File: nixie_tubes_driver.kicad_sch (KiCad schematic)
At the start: 3 parts, among them U5 CD40109BPW, U6 HV5122PG-G, U7 HV5122PG-G

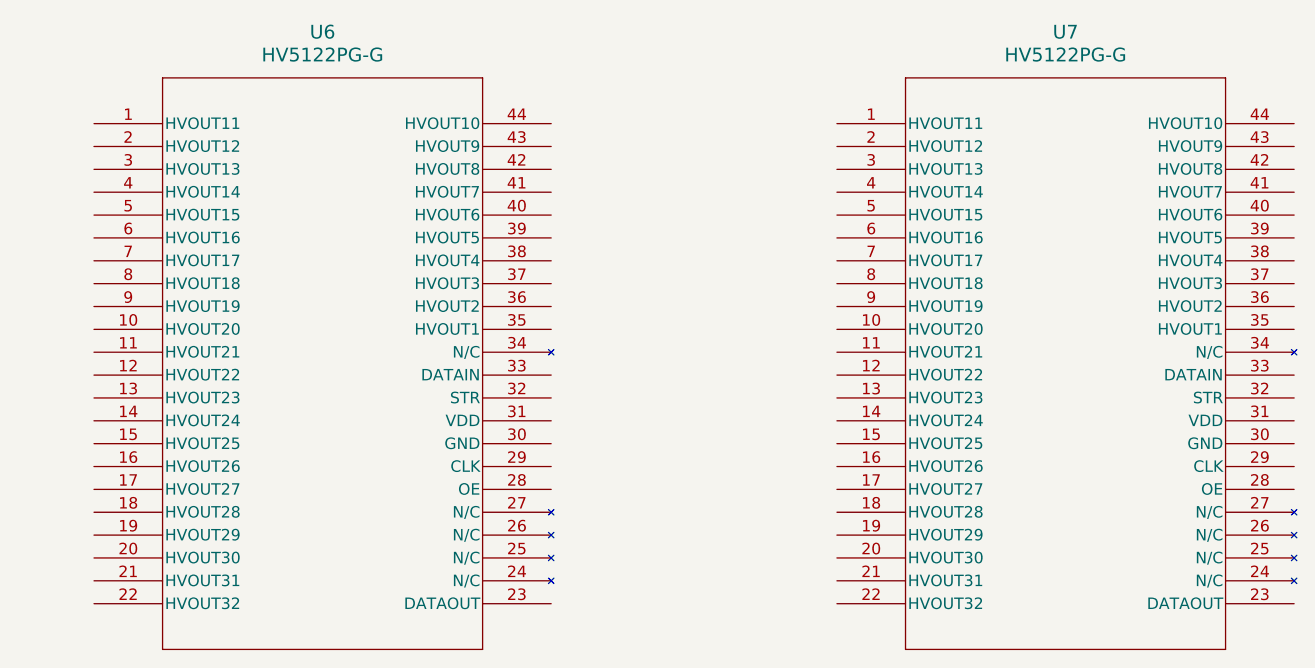
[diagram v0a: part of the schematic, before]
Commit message: Create symbol & footprint libraries
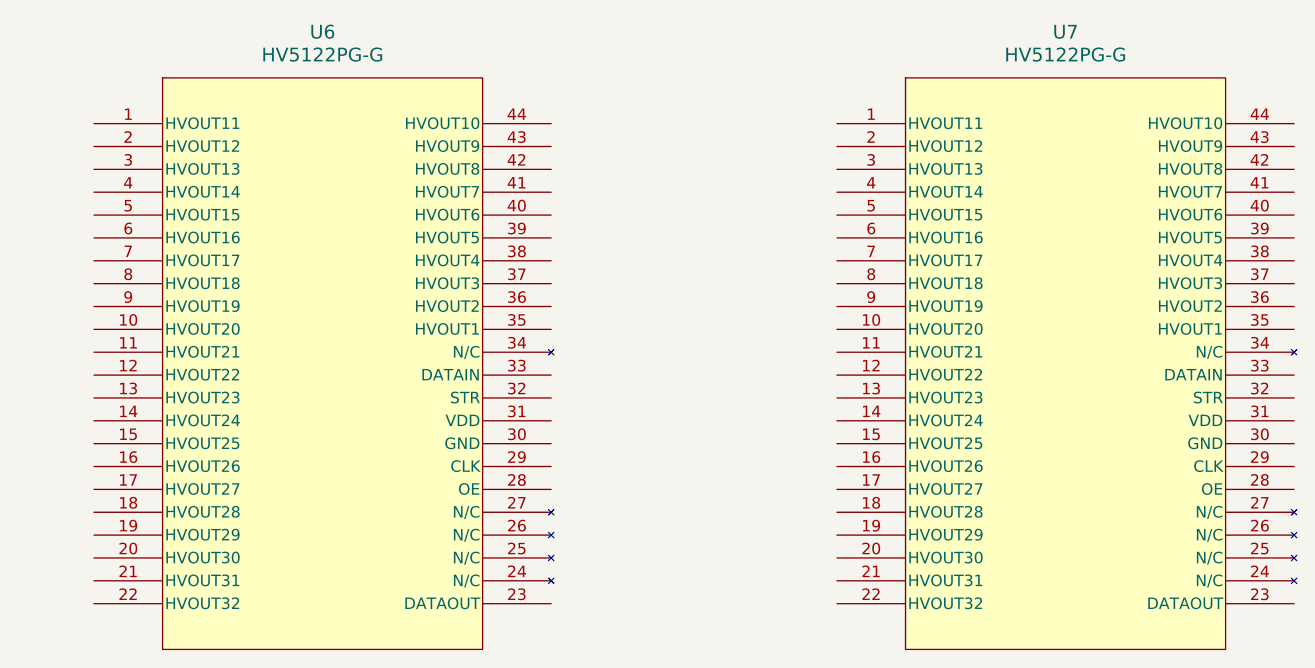
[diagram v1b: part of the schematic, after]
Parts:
- U6, U7: footprint HV5122PG-G:QFP44_10x10MC_MCH -> eclectronics_nixie_footprints:QFP44_10x10MC_MCH; symbol HV5122PG-G:HV5122PG-G -> electronics_nixie_lib:HV5122PG-G 32-Channel Shift Register; DigkeyPN (none) -> HV5122PG-G-ND; LCSCPN (none) -> C637042; MFN (none) -> Microchip Technology; MPN (none) -> HV5122PG-G
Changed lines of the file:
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@@
 	(paper "A4")
 	(symbol
-		(lib_id "HV5122PG-G:HV5122PG-G")
+		(lib_id "electronics_nixie_lib:HV5122PG-G 32-Channel Shift Register ")
 		(at 93.98 77.47 0)
 		(unit 1)
@@
 			)
 		)
-		(property "Footprint" "HV5122PG-G:QFP44_10x10MC_MCH"
+		(property "Footprint" "eclectronics_nixie_footprints:QFP44_10x10MC_MCH"
 			(at 93.98 77.47 0)
 			(effects
@@
 			)
 		)
-		(property "Datasheet" "HV5122PG-G"
+		(property "Datasheet" "https://ww1.microchip.com/downloads/en/DeviceDoc/20005418B.pdf"
 			(at 93.98 77.47 0)
 			(effects
@@
 		)
 		(property "Description" ""
+			(at 93.98 77.47 0)
+			(effects
+				(font
+					(size 1.27 1.27)
+				)
+				(hide yes)
+			)
+		)
+		(property "MFN" "Microchip Technology"
+			(at 93.98 77.47 0)
+			(effects
+				(font
+					(size 1.27 1.27)
+				)
+				(hide yes)
+			)
+		)
+		(property "MPN" "HV5122PG-G"
+			(at 93.98 77.47 0)
+			(effects
+				(font
+					(size 1.27 1.27)
+				)
+				(hide yes)
+			)
+		)
+		(property "DigkeyPN" "HV5122PG-G-ND"
+			(at 93.98 77.47 0)
+			(effects
+				(font
+					(size 1.27 1.27)
+				)
+				(hide yes)
+			)
+		)
+		(property "LCSCPN" "C637042"
 			(at 93.98 77.47 0)
 			(effects
@@
 	)
 	(symbol
-		(lib_id "HV5122PG-G:HV5122PG-G")
+		(lib_id "electronics_nixie_lib:HV5122PG-G 32-Channel Shift Register ")
 		(at 176.53 77.47 0)
 		(unit 1)
@@
 			)
 		)
-		(property "Footprint" "HV5122PG-G:QFP44_10x10MC_MCH"
+		(property "Footprint" "eclectronics_nixie_footprints:QFP44_10x10MC_MCH"
 			(at 176.53 77.47 0)
 			(effects
@@
 			)
 		)
-		(property "Datasheet" "HV5122PG-G"
+		(property "Datasheet" "https://ww1.microchip.com/downloads/en/DeviceDoc/20005418B.pdf"
 			(at 176.53 77.47 0)
 			(effects
@@
 			(at 176.53 77.47 0)
 			(effects
+				(font
+					(size 1.27 1.27)
+				)
+				(hide yes)
+			)
+		)
+		(property "MFN" "Microchip Technology"
+			(at 176.53 77.47 0)
+			(effects
+				(font
+					(size 1.27 1.27)
+				)
+				(hide yes)
+			)
+		)
+		(property "MPN" "HV5122PG-G"
+			(at 176.53 77.47 0)
+			(effects
+				(font
+					(size 1.27 1.27)
+				)
+				(hide yes)
+			)
+		)
+		(property "DigkeyPN" "HV5122PG-G-ND"
+			(at 176.53 77.47 0)
+			(effects
+				(font
+					(size 1.27 1.27)
+				)
+				(hide yes)
+			)
+		)
+		(property "LCSCPN" "C637042"
+			(at 176.53 77.47 0)
+			(effects

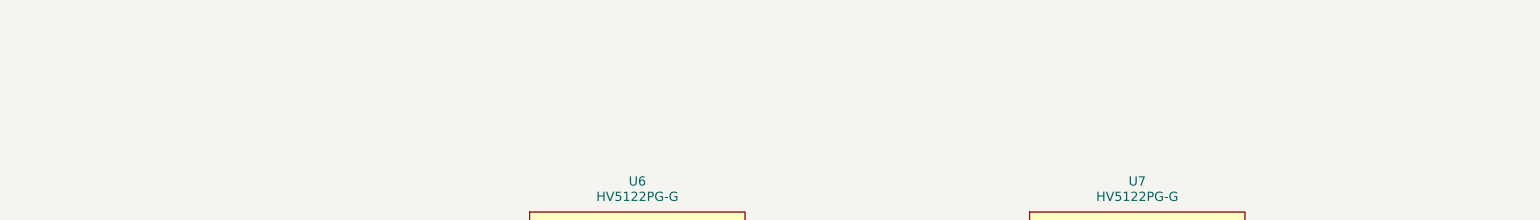
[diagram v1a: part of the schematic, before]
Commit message: Add current limiting resistors and net labels to nixie tubes
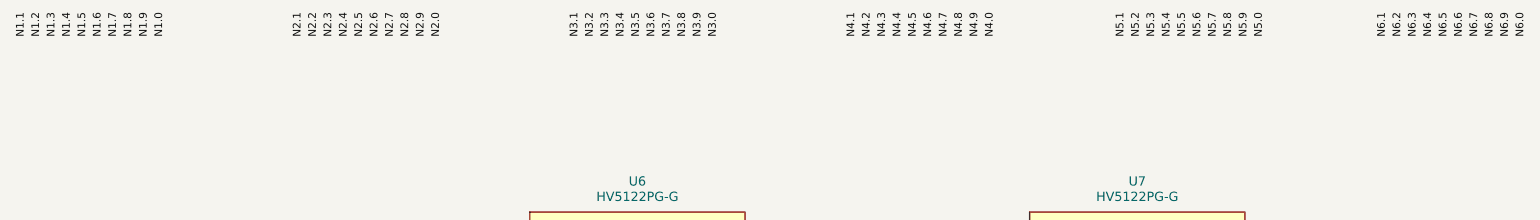
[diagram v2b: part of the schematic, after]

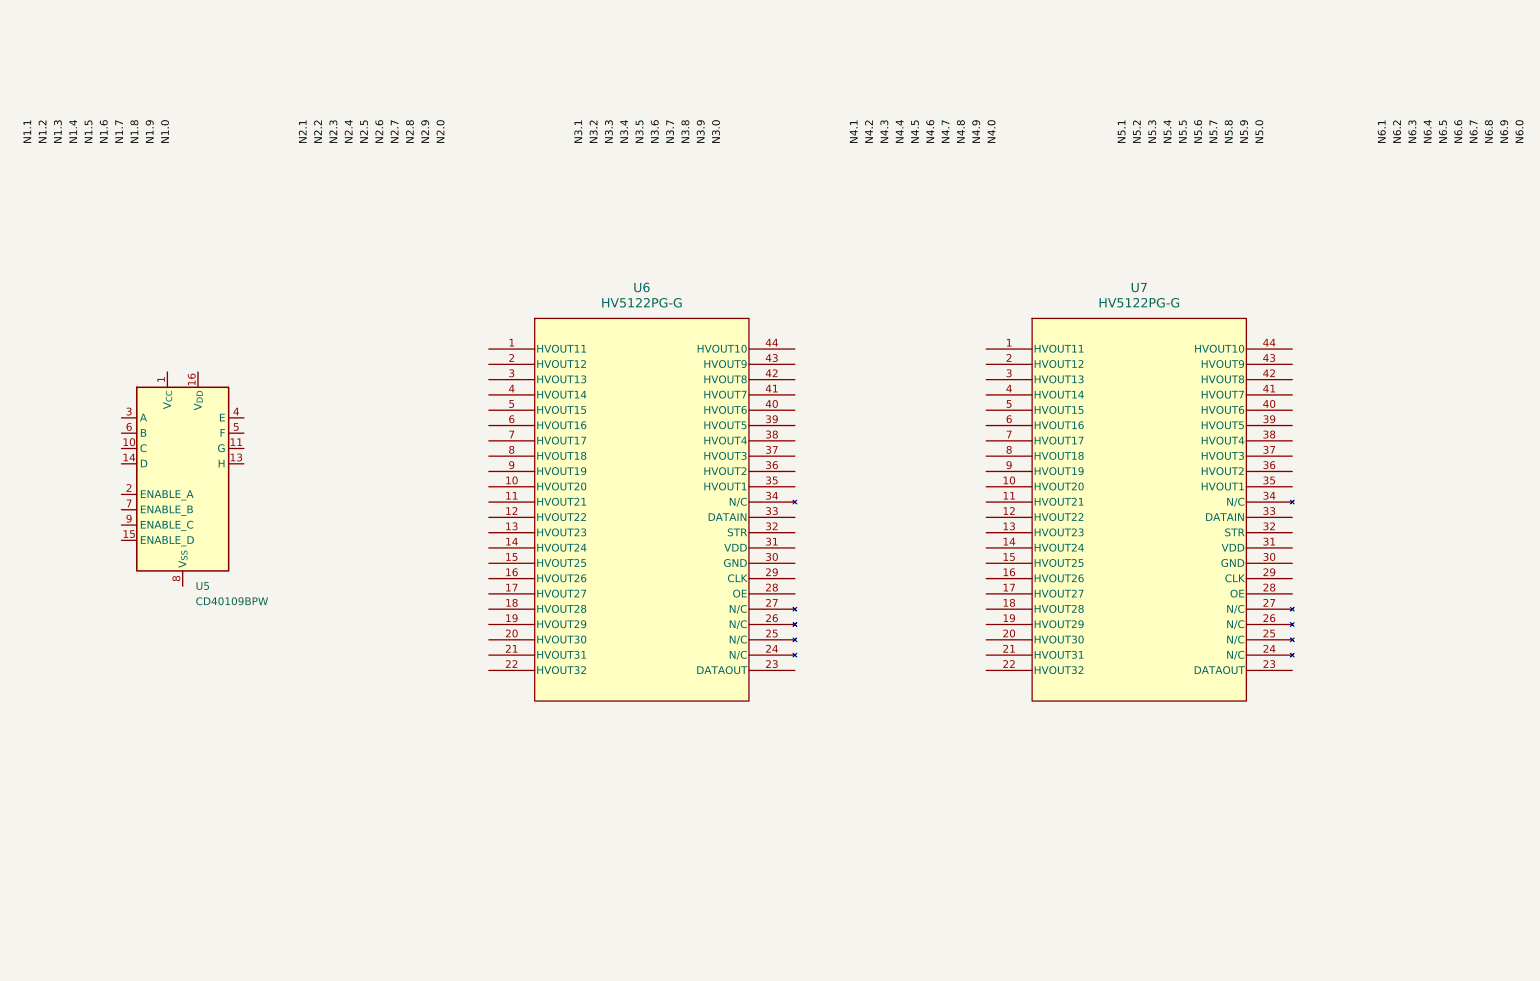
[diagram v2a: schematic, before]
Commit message: Add nixie tube net labels and dc/dc converter
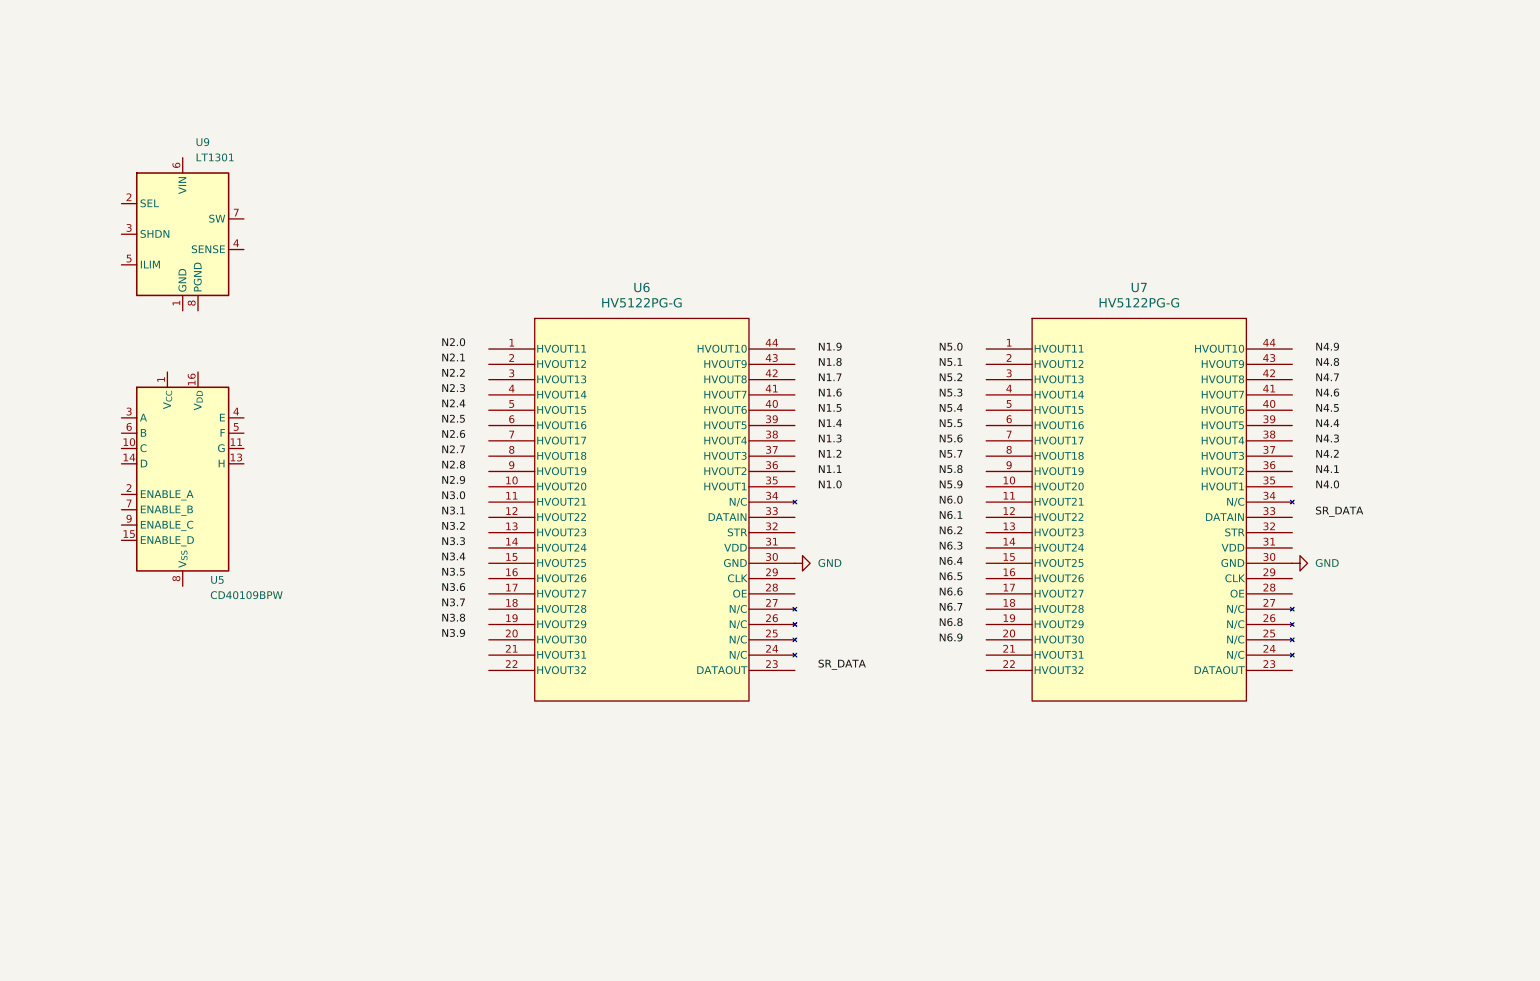
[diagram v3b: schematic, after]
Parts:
- added U9: LT1301, symbol Regulator_Switching:LT1301
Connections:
- net GND: now reaches U6.30 (GND)
- net GND: now also U7.30 (GND)

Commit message: Add more net labels to driver
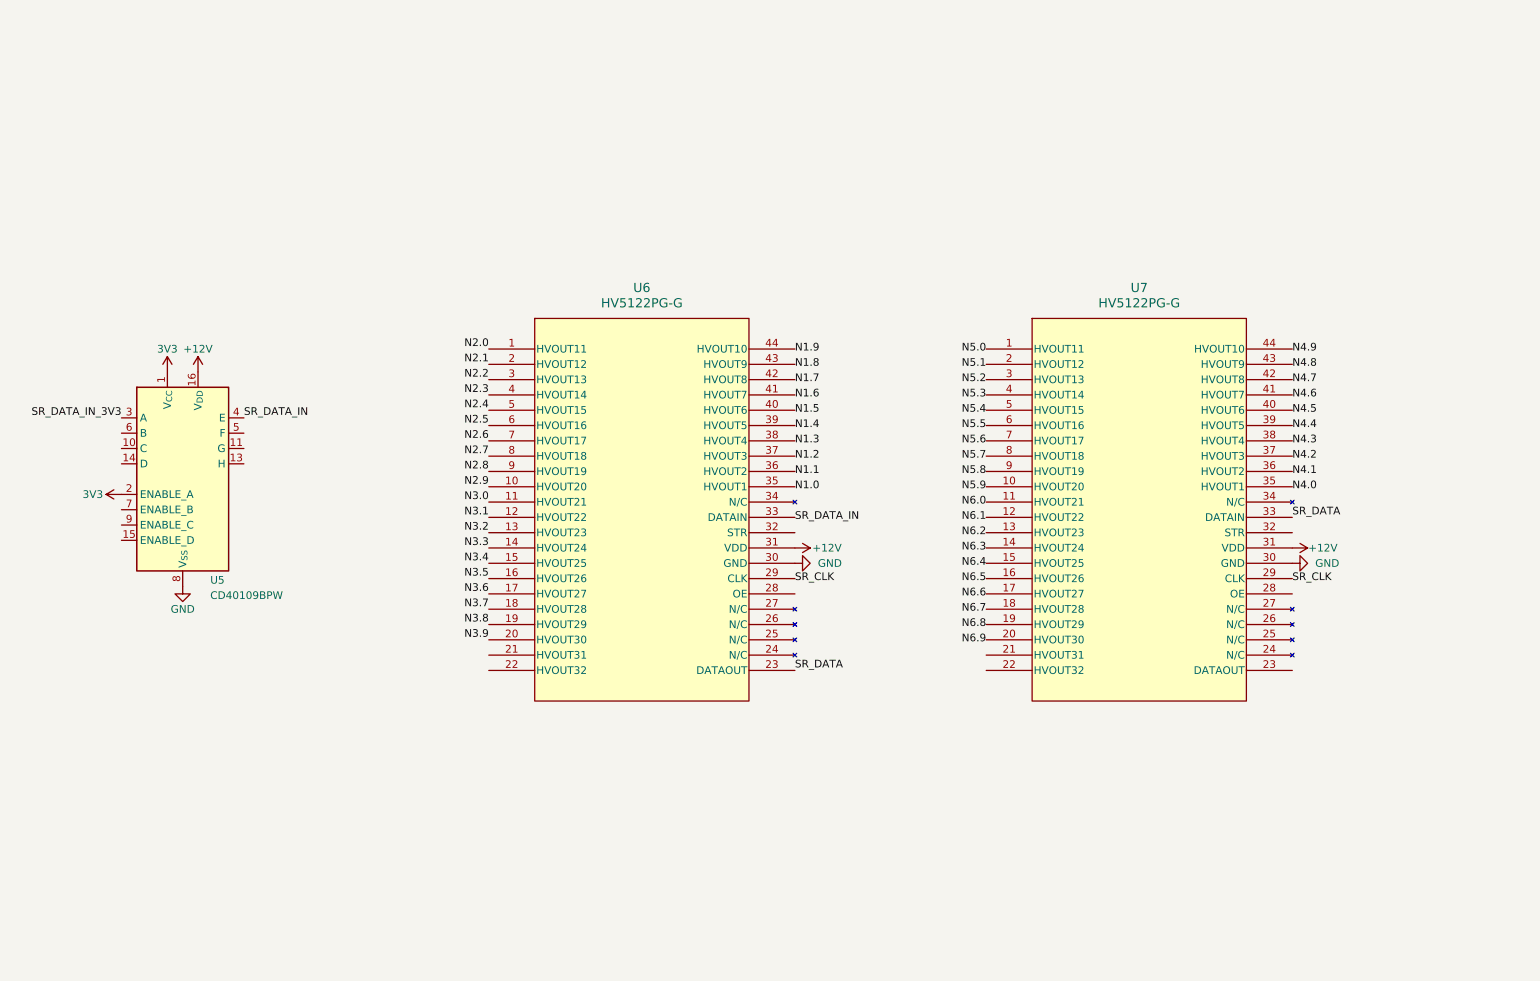
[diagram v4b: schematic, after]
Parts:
- removed U9: LT1301, symbol Regulator_Switching:LT1301
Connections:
- net GND: now also U5.8 (V_{SS})
- net N1.0: now also U6.35 (HVOUT1)
- net N1.1: now also U6.36 (HVOUT2)
- net N1.2: now also U6.37 (HVOUT3)
- net N1.3: now also U6.38 (HVOUT4)
- net N1.4: now also U6.39 (HVOUT5)
- net N1.5: now also U6.40 (HVOUT6)
- net N1.6: now also U6.41 (HVOUT7)
- net N1.7: now also U6.42 (HVOUT8)
- net N1.8: now also U6.43 (HVOUT9)
- net N1.9: now also U6.44 (HVOUT10)
- net N2.0: now also U6.1 (HVOUT11)
- net N2.1: now also U6.2 (HVOUT12)
- net N2.2: now also U6.3 (HVOUT13)
- net N2.3: now also U6.4 (HVOUT14)
- net N2.4: now also U6.5 (HVOUT15)
- net N2.5: now also U6.6 (HVOUT16)
- net N2.6: now also U6.7 (HVOUT17)
- net N2.7: now also U6.8 (HVOUT18)
- net N2.8: now also U6.9 (HVOUT19)
- net N2.9: now also U6.10 (HVOUT20)
- net N3.0: now also U6.11 (HVOUT21)
- net N3.1: now also U6.12 (HVOUT22)
- net N3.2: now also U6.13 (HVOUT23)
- net N3.3: now also U6.14 (HVOUT24)
- net N3.4: now also U6.15 (HVOUT25)
- net N3.5: now also U6.16 (HVOUT26)
- net N3.6: now also U6.17 (HVOUT27)
- net N3.7: now also U6.18 (HVOUT28)
- net N3.8: now also U6.19 (HVOUT29)
- net N3.9: now also U6.20 (HVOUT30)
- net N4.0: now also U7.35 (HVOUT1)
- net N4.1: now also U7.36 (HVOUT2)
- net N4.2: now also U7.37 (HVOUT3)
- net N4.3: now also U7.38 (HVOUT4)
- net N4.4: now also U7.39 (HVOUT5)
- net N4.5: now also U7.40 (HVOUT6)
- net N4.6: now also U7.41 (HVOUT7)
- net N4.7: now also U7.42 (HVOUT8)
- net N4.8: now also U7.43 (HVOUT9)
- net N4.9: now also U7.44 (HVOUT10)
- net N5.0: now also U7.1 (HVOUT11)
- net N5.1: now also U7.2 (HVOUT12)
- net N5.2: now also U7.3 (HVOUT13)
- net N5.3: now also U7.4 (HVOUT14)
- net N5.4: now also U7.5 (HVOUT15)
- net N5.5: now also U7.6 (HVOUT16)
- net N5.6: now also U7.7 (HVOUT17)
- net N5.7: now also U7.8 (HVOUT18)
- net N5.8: now also U7.9 (HVOUT19)
- net N5.9: now also U7.10 (HVOUT20)
- net N6.0: now also U7.11 (HVOUT21)
- net N6.1: now also U7.12 (HVOUT22)
- net N6.2: now also U7.13 (HVOUT23)
- net N6.3: now also U7.14 (HVOUT24)
- net N6.4: now also U7.15 (HVOUT25)
- net N6.5: now also U7.16 (HVOUT26)
- net N6.6: now also U7.17 (HVOUT27)
- net N6.7: now also U7.18 (HVOUT28)
- net N6.8: now also U7.19 (HVOUT29)
- net N6.9: now also U7.20 (HVOUT30)
- net SR_DATA: now also U6.23 (DATAOUT), U7.33 (DATAIN)
- net SR_CLK: now reaches U6.29 (CLK)
- net SR_CLK: now also U7.29 (CLK)
- net +12V: now reaches U6.31 (VDD)
- net +12V: now also U5.16 (V_{DD}), U7.31 (VDD)
- net SR_DATA_IN: now reaches U6.33 (DATAIN)
- net SR_DATA_IN: now also U5.4 (E)
- net 3V3: now reaches U5.1 (V_{CC})
- net 3V3: now also U5.2 (ENABLE_A)
- net SR_DATA_IN_3V3: now reaches U5.3 (A)
